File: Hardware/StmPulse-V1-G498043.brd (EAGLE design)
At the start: 60.3 x 128.5 mm, 63 parts, among them IC1 78M05, IC2 MCP6004D, T1_CLOCK 2N3904, T2_RESET TRANSISTOR_MMBT3904, U1 MCP6004D, U2-MCP4922 MCP4922MCP4922-SO14

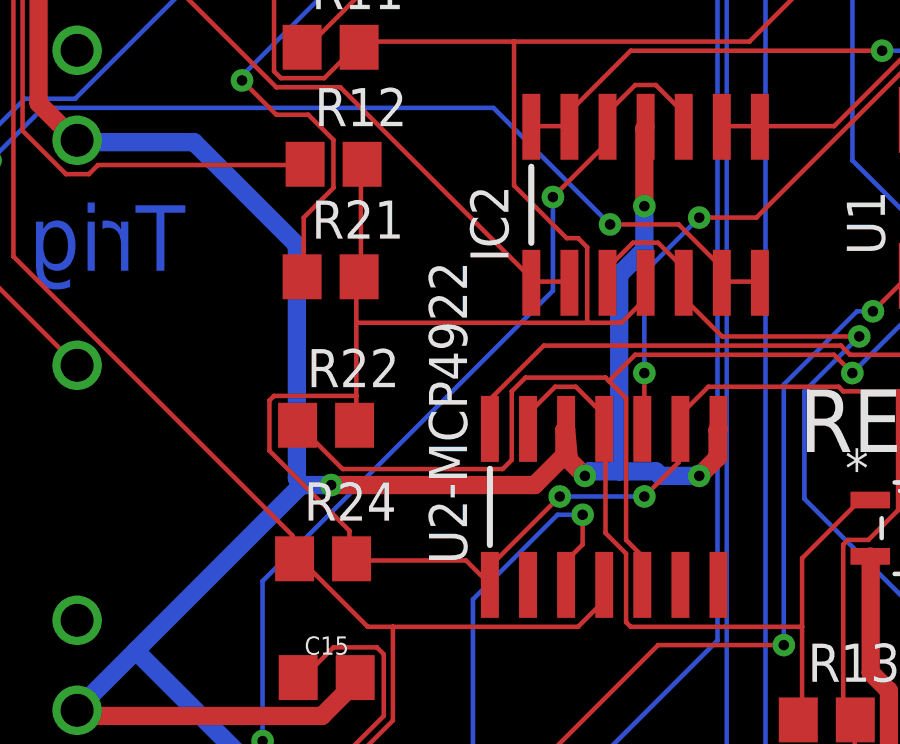
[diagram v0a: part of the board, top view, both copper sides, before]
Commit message: updated BOM and RS component
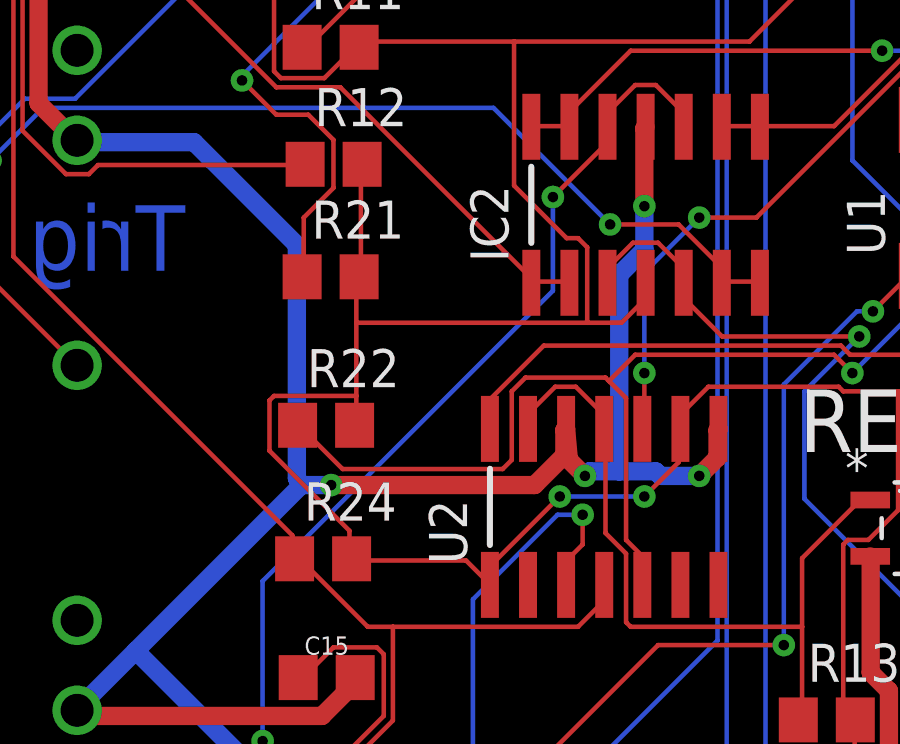
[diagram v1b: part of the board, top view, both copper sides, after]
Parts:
- renumbered U2-MCP4922 to U2
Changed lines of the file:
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@@
 <attribute name="NAME" x="139.362" y="18.049" size="0.4064" layer="104" rot="R90"/>
 <attribute name="PROD_ID" value="CONN-09508" x="128.44" y="20.97" size="1.778" layer="27" rot="R90" display="off"/>
+<attribute name="RS-PART" value="828-1783" x="128.44" y="20.97" size="1.778" layer="27" rot="R90" display="off"/>
 <attribute name="VALUE" x="118.026" y="18.049" size="0.4064" layer="27" font="vector" rot="R90"/>
 </element>
@@
 <attribute name="VALUE" x="99.79" y="50.56" size="1.016" layer="27"/>
 </element>
-<element name="U2-MCP4922" library="GMSN-R2Project" package="SO14" value="MCP4922MCP4922-SO14" x="102.37" y="63.28" smashed="yes">
+<element name="U2" library="GMSN-R2Project" package="SO14" value="MCP4922MCP4922-SO14" x="102.37" y="63.28" smashed="yes">
 <attribute name="NAME" x="97.798" y="61.375" size="1.27" layer="25" rot="R90"/>
 <attribute name="RS-PART" value="402-910 " x="78.24" y="62.01" size="1.778" layer="27" display="off"/>
@@
 <contactref element="C5" pad="2"/>
 <contactref element="U1" pad="11"/>
-<contactref element="U2-MCP4922" pad="8"/>
-<contactref element="U2-MCP4922" pad="12"/>
+<contactref element="U2" pad="8"/>
+<contactref element="U2" pad="12"/>
 <contactref element="C6" pad="2"/>
 <contactref element="C8" pad="2"/>
@@
 <contactref element="U1" pad="4"/>
 <contactref element="C5" pad="1"/>
-<contactref element="U2-MCP4922" pad="1"/>
-<contactref element="U2-MCP4922" pad="9"/>
+<contactref element="U2" pad="1"/>
+<contactref element="U2" pad="9"/>
 <contactref element="DISPLAY" pad="2"/>
 <contactref element="R13" pad="2"/>
@@
 <contactref element="DISPLAY" pad="4"/>
 <contactref element="U$1" pad="P$29"/>
-<contactref element="U2-MCP4922" pad="5"/>
+<contactref element="U2" pad="5"/>
 <contactref element="R22" pad="1"/>
 <wire x1="93.6498" y1="64.5414" x2="92.202" y2="65.9892" width="0.1524" layer="1"/>
@@
 <contactref element="DISPLAY" pad="3"/>
 <contactref element="U$1" pad="P$31"/>
-<contactref element="U2-MCP4922" pad="4"/>
+<contactref element="U2" pad="4"/>
 <contactref element="R24" pad="1"/>
 <wire x1="92.2782" y1="61.4934" x2="92.1258" y2="61.4934" width="0.1524" layer="1"/>
@@
 <signal name="VOUTA">
 <contactref element="U1" pad="10"/>
-<contactref element="U2-MCP4922" pad="14"/>
+<contactref element="U2" pad="14"/>
 <contactref element="U1" pad="3"/>
 <wire x1="98.6028" y1="66.9036" x2="98.6028" y2="65.913" width="0.1524" layer="1"/>
@@
 <signal name="VOUTB">
 <contactref element="U1" pad="12"/>
-<contactref element="U2-MCP4922" pad="10"/>
+<contactref element="U2" pad="10"/>
 <contactref element="U1" pad="5"/>
 <wire x1="103.7082" y1="67.7418" x2="103.7082" y2="65.913" width="0.1524" layer="1"/>
@@
 </signal>
 <signal name="CS1">
-<contactref element="U2-MCP4922" pad="3"/>
+<contactref element="U2" pad="3"/>
 <contactref element="U$1" pad="P$14"/>
 <wire x1="101.1174" y1="61.4934" x2="101.1174" y2="60.7314" width="0.1524" layer="1"/>
@@
 </signal>
 <signal name="3VREF">
-<contactref element="U2-MCP4922" pad="13"/>
-<contactref element="U2-MCP4922" pad="11"/>
+<contactref element="U2" pad="13"/>
+<contactref element="U2" pad="11"/>
 <contactref element="R13" pad="1"/>
 <contactref element="REF" pad="1"/>
